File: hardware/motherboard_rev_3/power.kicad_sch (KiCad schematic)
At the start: 22 parts, among them U10 TPS563201, U11 INA219AIDCN, U12 TPS7A8101

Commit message: Completed schematic for rev 3.0 PCB
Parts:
- R12: renamed from R17; LCSC (none) -> C601083
- renumbered C20 to C15, C21 to C16, C22 to C17, C23 to C18, C24 to C19, C25 to C20, C26 to C21, C27 to C22, C28 to C23, C29 to C24, R16 to R11, R18 to R13, R19 to R14, R20 to R15, R21 to R16, R22 to R17
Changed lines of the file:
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@@
 		(dnp no)
 		(fields_autoplaced yes)
-		(property "Reference" "#PWR054"
+		(property "Reference" "#PWR048"
 			(at 153.67 127 0)
 			(effects
@@
 			(project "wing_module_rev_1"
 				(path "/39c7ec0f-0a05-4172-b48a-dcc9b63f77ff/78f7b167-041e-41f6-8e25-c16c4d32d4b2"
-					(reference "#PWR054")
+					(reference "#PWR048")
 					(unit 1)
 				)
@@
 		(on_board yes)
 		(dnp no)
-		(property "Reference" "C22"
+		(property "Reference" "C17"
 			(at 115.57 49.53 90)
 			(effects
@@
 			(project "motherboard_rev_3"
 				(path "/39c7ec0f-0a05-4172-b48a-dcc9b63f77ff/78f7b167-041e-41f6-8e25-c16c4d32d4b2"
-					(reference "C22")
+					(reference "C17")
 					(unit 1)
 				)
@@
 		(on_board yes)
 		(dnp no)
-		(property "Reference" "R17"
+		(property "Reference" "R12"
 			(at 115.57 43.18 90)
 			(effects
@@
 			)
 		)
+		(property "LCSC" "C601083"
+			(at 115.57 45.72 90)
+			(effects
+				(font
+					(size 1.27 1.27)
+				)
+				(hide yes)
+			)
+		)
 		(pin "2"
 		)
@@
 			(project ""
 				(path "/39c7ec0f-0a05-4172-b48a-dcc9b63f77ff/78f7b167-041e-41f6-8e25-c16c4d32d4b2"
-					(reference "R17")
+					(reference "R12")
 					(unit 1)
 				)
@@
 		(on_board yes)
 		(dnp no)
-		(property "Reference" "C21"
+		(property "Reference" "C16"
 			(at 91.44 133.35 90)
 			(effects
@@
 			(project "wing_module_rev_1"
 				(path "/39c7ec0f-0a05-4172-b48a-dcc9b63f77ff/78f7b167-041e-41f6-8e25-c16c4d32d4b2"
-					(reference "C21")
+					(reference "C16")
 					(unit 1)
 				)
@@
 		(dnp no)
 		(fields_autoplaced yes)
-		(property "Reference" "#PWR048"
+		(property "Reference" "#PWR042"
 			(at 58.42 151.13 0)
 			(effects
@@
 			(project "wing_module_rev_1"
 				(path "/39c7ec0f-0a05-4172-b48a-dcc9b63f77ff/78f7b167-041e-41f6-8e25-c16c4d32d4b2"
-					(reference "#PWR048")
+					(reference "#PWR042")
 					(unit 1)
 				)
@@
 		(dnp no)
 		(fields_autoplaced yes)
-		(property "Reference" "C28"
+		(property "Reference" "C23"
 			(at 222.25 126.9999 0)
 			(effects
@@
 			(project "wing_module_rev_1"
 				(path "/39c7ec0f-0a05-4172-b48a-dcc9b63f77ff/78f7b167-041e-41f6-8e25-c16c4d32d4b2"
-					(reference "C28")
+					(reference "C23")
 					(unit 1)
 				)
@@
 		(on_board yes)
 		(dnp no)
-		(property "Reference" "R19"
+		(property "Reference" "R14"
 			(at 119.38 138.4299 0)
 			(effects
@@
 			(project "wing_module_rev_1"
 				(path "/39c7ec0f-0a05-4172-b48a-dcc9b63f77ff/78f7b167-041e-41f6-8e25-c16c4d32d4b2"
-					(reference "R19")
+					(reference "R14")
 					(unit 1)
 				)
@@
 		(on_board yes)
 		(dnp no)
-		(property "Reference" "R20"
+		(property "Reference" "R15"
 			(at 124.46 50.8 90)
 			(effects
@@
 			(project "motherboard_rev_3"
 				(path "/39c7ec0f-0a05-4172-b48a-dcc9b63f77ff/78f7b167-041e-41f6-8e25-c16c4d32d4b2"
-					(reference "R20")
+					(reference "R15")
 					(unit 1)
 				)
@@
 		(dnp no)
 		(fields_autoplaced yes)
-		(property "Reference" "#PWR050"
+		(property "Reference" "#PWR044"
 			(at 121.92 45.72 0)
 			(effects
@@
 			(project "motherboard_rev_3"
 				(path "/39c7ec0f-0a05-4172-b48a-dcc9b63f77ff/78f7b167-041e-41f6-8e25-c16c4d32d4b2"
-					(reference "#PWR050")
+					(reference "#PWR044")
 					(unit 1)
 				)
@@
 		(on_board yes)
 		(dnp no)
-		(property "Reference" "R18"
+		(property "Reference" "R13"
 			(at 119.38 128.2699 0)
 			(effects
@@
 			(project "wing_module_rev_1"
 				(path "/39c7ec0f-0a05-4172-b48a-dcc9b63f77ff/78f7b167-041e-41f6-8e25-c16c4d32d4b2"
-					(reference "R18")
+					(reference "R13")
 					(unit 1)
 				)
@@
 		(dnp no)
 		(fields_autoplaced yes)
-		(property "Reference" "#PWR055"
+		(property "Reference" "#PWR049"
 			(at 232.41 124.46 0)
 			(effects
@@
 			(project "wing_module_rev_1"
 				(path "/39c7ec0f-0a05-4172-b48a-dcc9b63f77ff/78f7b167-041e-41f6-8e25-c16c4d32d4b2"
-					(reference "#PWR055")
+					(reference "#PWR049")
 					(unit 1)
 				)
@@
 		(dnp no)
 		(fields_autoplaced yes)
-		(property "Reference" "#PWR052"
+		(property "Reference" "#PWR046"
 			(at 153.67 60.96 0)
 			(effects
@@
 			(project "motherboard_rev_3"
 				(path "/39c7ec0f-0a05-4172-b48a-dcc9b63f77ff/78f7b167-041e-41f6-8e25-c16c4d32d4b2"
-					(reference "#PWR052")
+					(reference "#PWR046")
 					(unit 1)
 				)
@@
 		(on_board yes)
 		(dnp no)
-		(property "Reference" "C27"
+		(property "Reference" "C22"
 			(at 177.8 135.89 0)
 			(effects
@@
 			(project "wing_module_rev_1"
 				(path "/39c7ec0f-0a05-4172-b48a-dcc9b63f77ff/78f7b167-041e-41f6-8e25-c16c4d32d4b2"
-					(reference "C27")
+					(reference "C22")
 					(unit 1)
 				)
@@
 		(on_board yes)
 		(dnp no)
-		(property "Reference" "C26"
+		(property "Reference" "C21"
 			(at 163.83 133.3499 0)
 			(effects
@@
 			(project "wing_module_rev_1"
 				(path "/39c7ec0f-0a05-4172-b48a-dcc9b63f77ff/78f7b167-041e-41f6-8e25-c16c4d32d4b2"
-					(reference "C26")
+					(reference "C21")
 					(unit 1)
 				)
@@
 		(dnp no)
 		(fields_autoplaced yes)
-		(property "Reference" "C24"
+		(property "Reference" "C19"
 			(at 146.05 60.9599 0)
 			(effects
@@
 			(project "motherboard_rev_3"
 				(path "/39c7ec0f-0a05-4172-b48a-dcc9b63f77ff/78f7b167-041e-41f6-8e25-c16c4d32d4b2"
-					(reference "C24")
+					(reference "C19")
 					(unit 1)
 				)
@@
 		(on_board yes)
 		(dnp no)
-		(property "Reference" "C23"
+		(property "Reference" "C18"
 			(at 133.35 133.3499 0)
 			(effects
@@
 			(project "wing_module_rev_1"
 				(path "/39c7ec0f-0a05-4172-b48a-dcc9b63f77ff/78f7b167-041e-41f6-8e25-c16c4d32d4b2"
-					(reference "C23")
+					(reference "C18")
 					(unit 1)
 				)
@@
 		(on_board yes)
 		(dnp no)
-		(property "Reference" "C25"
+		(property "Reference" "C20"
 			(at 146.05 133.3499 0)
 			(effects
@@
 			(project "wing_module_rev_1"
 				(path "/39c7ec0f-0a05-4172-b48a-dcc9b63f77ff/78f7b167-041e-41f6-8e25-c16c4d32d4b2"
-					(reference "C25")
+					(reference "C20")
 					(unit 1)
 				)
@@
 		(on_board yes)
 		(dnp no)
-		(property "Reference" "R16"
+		(property "Reference" "R11"
 			(at 106.68 50.8 90)
 			(effects
@@
 			(project "motherboard_rev_3"
 				(path "/39c7ec0f-0a05-4172-b48a-dcc9b63f77ff/78f7b167-041e-41f6-8e25-c16c4d32d4b2"
-					(reference "R16")
+					(reference "R11")
 					(unit 1)
 				)
@@
 		(dnp no)
 		(fields_autoplaced yes)
-		(property "Reference" "#PWR051"
+		(property "Reference" "#PWR045"
 			(at 142.24 72.39 0)
 			(effects
@@
 			(project "motherboard_rev_3"
 				(path "/39c7ec0f-0a05-4172-b48a-dcc9b63f77ff/78f7b167-041e-41f6-8e25-c16c4d32d4b2"
-					(reference "#PWR051")
+					(reference "#PWR045")
 					(unit 1)
 				)
@@
 		(on_board yes)
 		(dnp no)
-		(property "Reference" "R22"
+		(property "Reference" "R17"
 			(at 214.63 137.1599 0)
 			(effects
@@
 			(project "wing_module_rev_1"
 				(path "/39c7ec0f-0a05-4172-b48a-dcc9b63f77ff/78f7b167-041e-41f6-8e25-c16c4d32d4b2"
-					(reference "R22")
+					(reference "R17")
 					(unit 1)
 				)
@@
 		(dnp no)
 		(fields_autoplaced yes)
-		(property "Reference" "#PWR049"
+		(property "Reference" "#PWR043"
 			(at 100.33 66.04 0)
 			(effects
@@
 			(project "motherboard_rev_3"
 				(path "/39c7ec0f-0a05-4172-b48a-dcc9b63f77ff/78f7b167-041e-41f6-8e25-c16c4d32d4b2"
-					(reference "#PWR049")
+					(reference "#PWR043")
 					(unit 1)
 				)
@@
 		(on_board yes)
 		(dnp no)
-		(property "Reference" "C29"
+		(property "Reference" "C24"
 			(at 234.95 133.3499 0)
 			(effects
@@
 			(project "wing_module_rev_1"
 				(path "/39c7ec0f-0a05-4172-b48a-dcc9b63f77ff/78f7b167-041e-41f6-8e25-c16c4d32d4b2"
-					(reference "C29")
+					(reference "C24")
 					(unit 1)
 				)
@@
 		(on_board yes)
 		(dnp no)
-		(property "Reference" "C20"
+		(property "Reference" "C15"
 			(at 54.61 133.3499 0)
 			(effects
@@
 			(project "wing_module_rev_1"
 				(path "/39c7ec0f-0a05-4172-b48a-dcc9b63f77ff/78f7b167-041e-41f6-8e25-c16c4d32d4b2"
-					(reference "C20")
+					(reference "C15")
 					(unit 1)
 				)
@@
 		(on_board yes)
 		(dnp no)
-		(property "Reference" "R21"
+		(property "Reference" "R16"
 			(at 209.55 126.9999 0)
 			(effects
@@
 			(project "wing_module_rev_1"
 				(path "/39c7ec0f-0a05-4172-b48a-dcc9b63f77ff/78f7b167-041e-41f6-8e25-c16c4d32d4b2"
-					(reference "R21")
+					(reference "R16")
 					(unit 1)
 				)
@@
 		(dnp no)
 		(fields_autoplaced yes)
-		(property "Reference" "#PWR047"
+		(property "Reference" "#PWR041"
 			(at 58.42 125.73 0)
 			(effects
@@
 			(project "wing_module_rev_1"
 				(path "/39c7ec0f-0a05-4172-b48a-dcc9b63f77ff/78f7b167-041e-41f6-8e25-c16c4d32d4b2"
-					(reference "#PWR047")
+					(reference "#PWR041")
 					(unit 1)
 				)
@@
 		(dnp no)
 		(fields_autoplaced yes)
-		(property "Reference" "#PWR053"
+		(property "Reference" "#PWR047"
 			(at 153.67 96.52 0)
 			(effects
@@
 			(project ""
 				(path "/39c7ec0f-0a05-4172-b48a-dcc9b63f77ff/78f7b167-041e-41f6-8e25-c16c4d32d4b2"
-					(reference "#PWR053")
-					(unit 1)
-				)
+					(reference "#PWR047")
+					(unit 1)
+				)

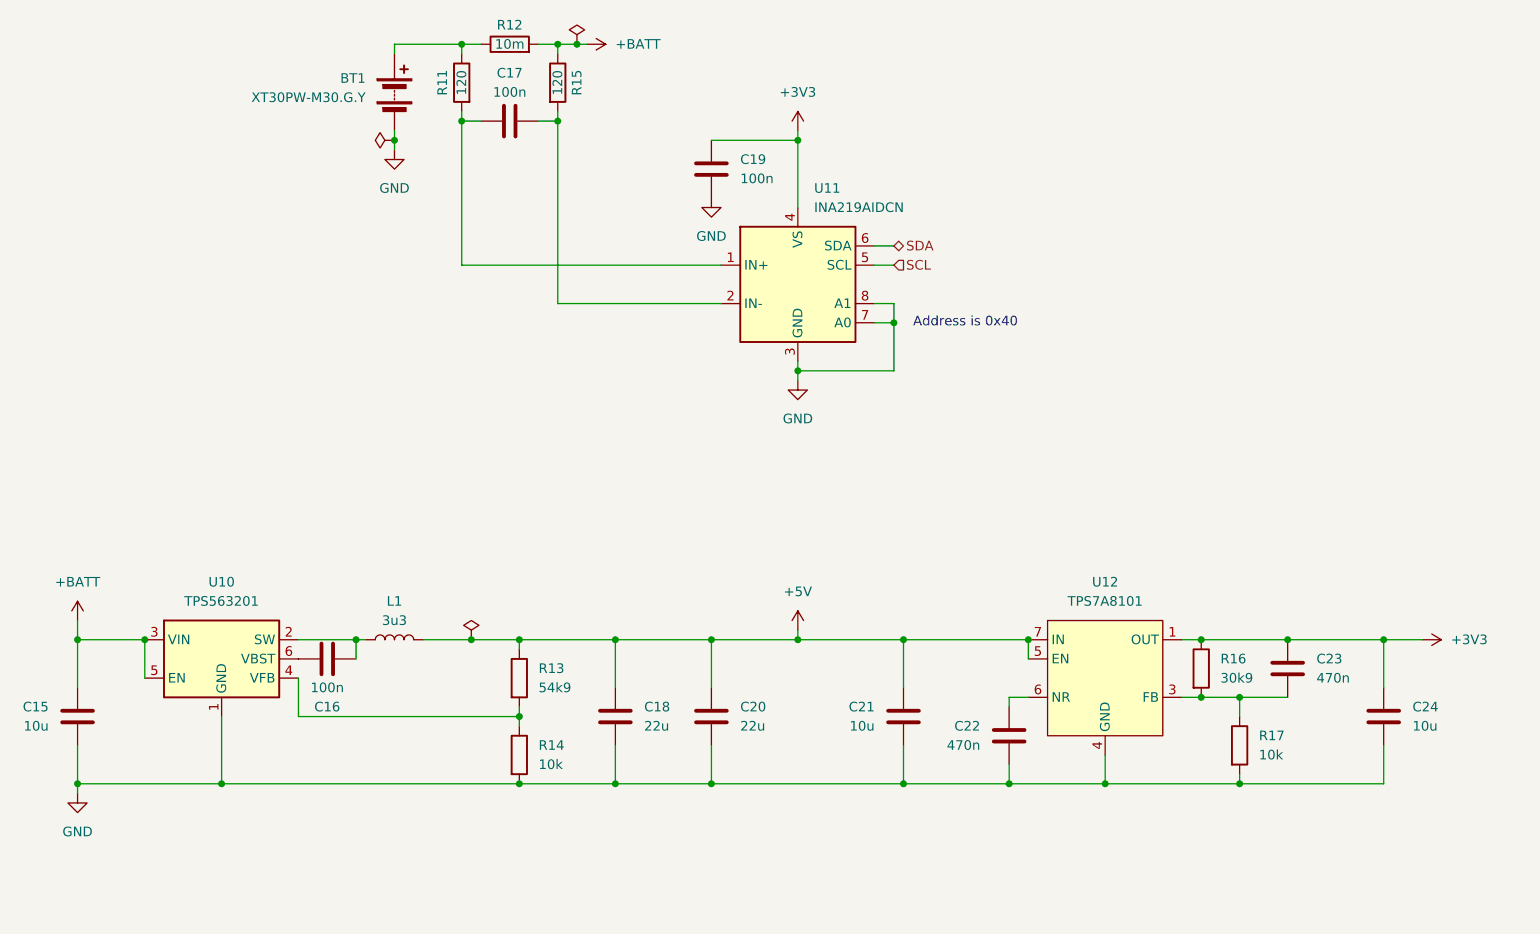
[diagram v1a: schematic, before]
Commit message: Removed LDO and just regulate to 3.3V, also removed off board CO2
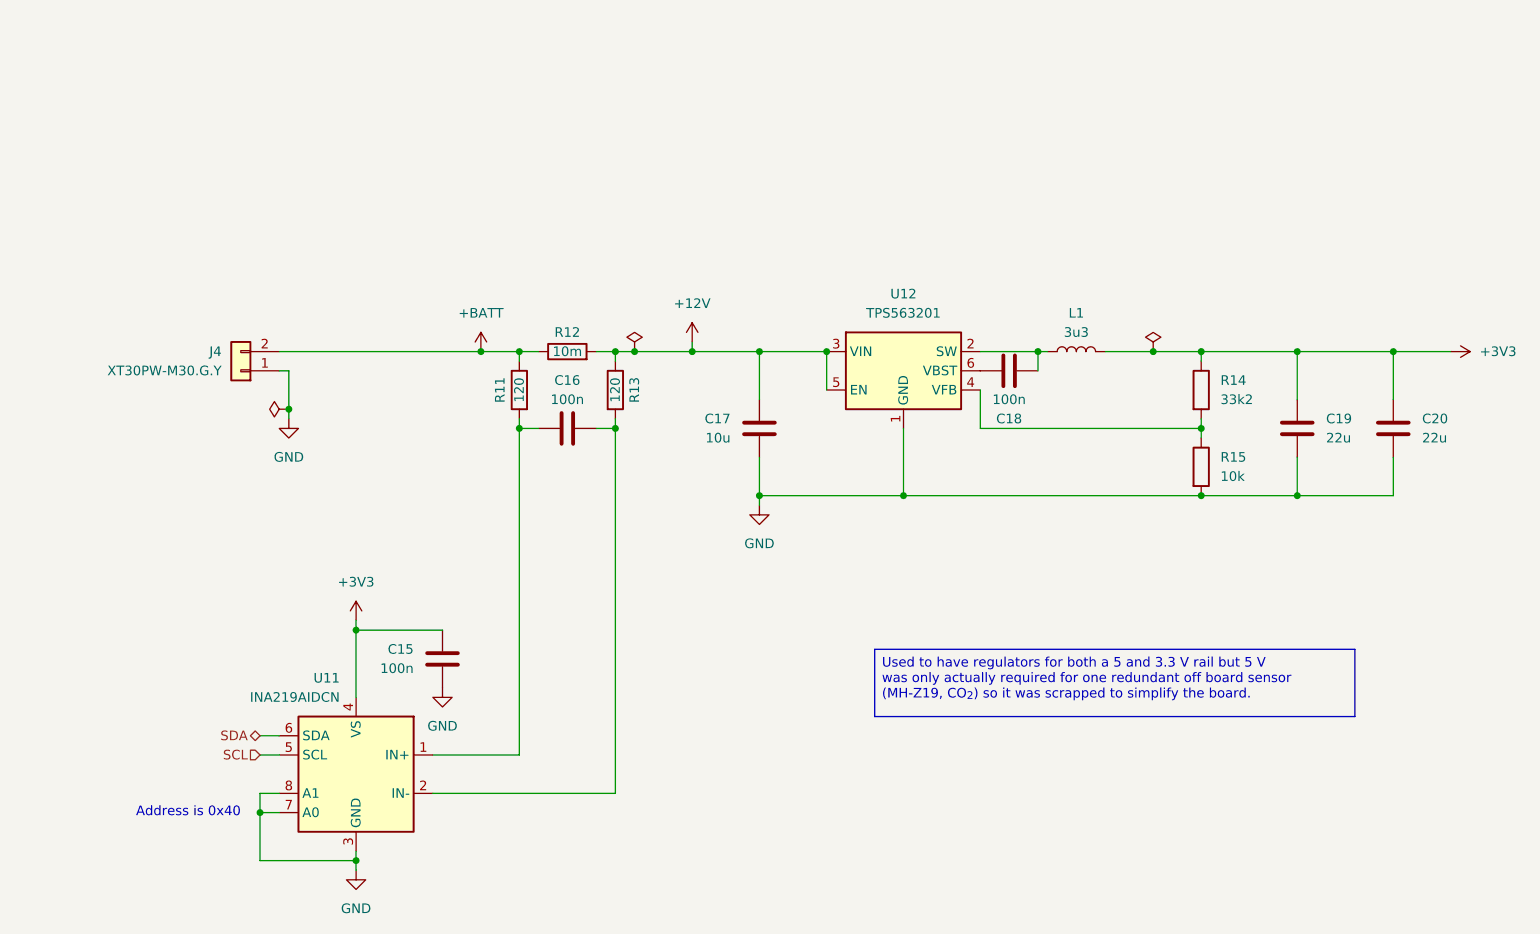
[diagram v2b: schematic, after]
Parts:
- removed C21, C24: 10u, Capacitor_SMD:C_0603_1608Metric, symbol Device:C
- removed C22, C23: 470n, Capacitor_SMD:C_0402_1005Metric, symbol Device:C
- removed R16: 30k9, Resistor_SMD:R_0402_1005Metric, symbol Device:R
- removed R17: 10k, Resistor_SMD:R_0402_1005Metric, symbol Device:R
- removed U12: TPS7A8101, Package_SON:VSON-8-1EP_3x3mm_P0.65mm_EP1.65x2.4mm, symbol mb_sensors:TPS7A8101
- J4: renamed from BT1; symbol Device:Battery -> Connector_Generic:Conn_01x02
- R14: renamed from R13; value 54k9 -> 33k2; LCSC C227137 -> C122548
- renumbered C19 to C15, C17 to C16, C15 to C17, C16 to C18, C18 to C19, R15 to R13, R14 to R15, U10 to U12
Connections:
- net +5V is gone; now on net +3V3: C19.1, C20.1, L1.2, R14.1
- net +BATT: now also J4.2 (Pin_2), R11.1, R12.1; no longer C17.1, R12.2, R13.1, U12.3 (VIN), U12.5 (EN)
- net GND: now also J4.1 (Pin_1); no longer J4.2 (-)
- new net +12V: C17.1, R12.2, R13.1, U12.3 (VIN), U12.5 (EN)
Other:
- moved on the sheet: C15, C16, C17, C18, C19, C20, L1, R11, R12, R13, R14, R15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

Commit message: Motherboard rev 3.1 as ordered
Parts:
- C15, C16, C18: LCSC C5448875 -> C301928
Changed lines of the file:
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@@
 		(company "Savo Bajic")
 		(comment 1 "Provides 3.3 V and includes a power monitoring IC")
+		(comment 2 "Handles up to 17 V input (limited by convertor IC)")
 	)
 	(text "Address is 0x40"
@@
 			)
 		)
-		(property "LCSC" "C5448875"
+		(property "LCSC" "C301928"
 			(at 123.19 96.52 0)
 			(effects
@@
 			)
 		)
-		(property "LCSC" "C5448875"
+		(property "LCSC" "C301928"
 			(at 181.61 88.9 0)
 			(effects
@@
 			)
 		)
-		(property "LCSC" "C5448875"
+		(property "LCSC" "C301928"
 			(at 106.68 127 0)
 			(effects
